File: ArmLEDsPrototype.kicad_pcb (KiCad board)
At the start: 2 copper layers, 11 parts

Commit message: Making PCB
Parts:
- added C10: C, Capacitor_SMD:C_0201_0603Metric_Pad0.64x0.40mm_HandSolder, F.Cu at (137.5, 25.7)
- added C11: C, Capacitor_SMD:C_0805_2012Metric_Pad1.18x1.45mm_HandSolder, F.Cu at (136.7, 22.5)
- added C12: C, Capacitor_SMD:C_0805_2012Metric_Pad1.18x1.45mm_HandSolder, F.Cu at (134.7, 22.5)
- added C6: C, Capacitor_SMD:C_0201_0603Metric_Pad0.64x0.40mm_HandSolder, F.Cu at (119.6, 25.2)
- added C7: C, Capacitor_SMD:C_0805_2012Metric_Pad1.18x1.45mm_HandSolder, F.Cu at (118.8, 22.0)
- added C8: C, Capacitor_SMD:C_0805_2012Metric_Pad1.18x1.45mm_HandSolder, F.Cu at (116.8, 22.0)
- added C9: C, Capacitor_SMD:C_1812_4532Metric_Pad1.57x3.40mm_HandSolder, F.Cu at (134.2, 30.4)
- added L2: L, ArmLEDFootprintLib:4r7007, F.Cu at (120.2, 23.7)
- added L3: L, ArmLEDFootprintLib:4r7007, F.Cu at (138.1, 24.2)
- added R12: R, Resistor_SMD:R_0402_1005Metric_Pad0.72x0.64mm_HandSolder, F.Cu at (114.8, 25.6)
- added R13: R, Resistor_SMD:R_0402_1005Metric_Pad0.72x0.64mm_HandSolder, F.Cu at (132.8, 23.6)
- added R14: R, Resistor_SMD:R_0402_1005Metric_Pad0.72x0.64mm_HandSolder, F.Cu at (132.7, 26.1)
- added U2: ~, ArmLEDFootprintLib:RT6254A, F.Cu at (117.2, 25.7)
- added U3: ~, ArmLEDFootprintLib:RT6254A, F.Cu at (135.1, 26.2)
- C1, C5: footprint Capacitor_SMD:C_0805_2012Metric_Pad1.18x1.45mm_HandSolder -> Capacitor_SMD:C_1812_4532Metric_Pad1.57x3.40mm_HandSolder
- L1: footprint ArmLEDFootprintLib:Inductor -> ArmLEDFootprintLib:4r7007
- moved C3 36.7 mm to (100.3, 21.2), turned to 90 degrees
- moved R10 36.2 mm to (96.3, 24.8), turned to -90 degrees
- moved R11 19.7 mm to (114.9, 23.1), turned to -90 degrees
- moved C5 17.9 mm to (116.3, 29.9), turned to 180 degrees
- moved C1 17.3 mm to (97.8, 29.1), turned to 180 degrees
- moved U1 17.2 mm to (98.7, 24.9)
- moved R9 14.9 mm to (96.4, 22.3)
- moved C4 12.3 mm to (98.3, 21.2), turned to 90 degrees
- moved L1 12.2 mm to (101.7, 22.9), turned to 90 degrees
- moved C2 10.8 mm to (101.1, 24.4), turned to -90 degrees
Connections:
- A1 pad 30: +5V -> /5V#1
- C3 pad 1: +5V -> /5V#1
- C3 pad 2: Net-(C3-Pad2) -> GND
- C4 pad 1: +5V -> /5V#1
- C5 pad 1: +5V -> +9V
- L1 pad 2: +5V -> /5V#1
- R10 pad 1: +5V -> Net-(U1-FB)
- R10 pad 2: Net-(C3-Pad2) -> GND
- R11 pad 1: GND -> /5V#2
- R11 pad 2: Net-(C3-Pad2) -> Net-(U2-FB)
- R9 pad 1: Net-(U1-FB) -> /5V#1
- R9 pad 2: Net-(C3-Pad2) -> Net-(U1-FB)
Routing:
- net +9V: track 0.00 -> 17.9 mm
- net /5V#2: track 0.00 -> 9.73 mm
- net /5V#1: track 0.00 -> 9.73 mm
- net /5V#3: track 0.00 -> 9.73 mm
- net Net-(U1-LX): track 0.00 -> 5.51 mm
- net Net-(U3-LX): track 0.00 -> 5.51 mm
- net Net-(U2-LX): track 0.00 -> 5.51 mm
- net Net-(U2-BOOT): track 0.00 -> 1.12 mm
- net Net-(U3-BOOT): track 0.00 -> 1.12 mm
- net Net-(U1-BOOT): track 0.00 -> 1.12 mm
- added copper zone on F.Cu, net GND
- added copper zone on F.Cu, net Net-(U1-LX)

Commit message: Added parts
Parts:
- added J3: Conn_01x02, Connector_Molex:Molex_Pico-EZmate_78171-0002_1x02-1MP_P1.20mm_Vertical, F.Cu at (109.2, 32.9)
- added J5: Conn_01x03, Connector_Molex:Molex_Pico-EZmate_78171-0003_1x03-1MP_P1.20mm_Vertical, F.Cu at (117.5, 32.9)
- added J6: Conn_01x02, Connector_Molex:Molex_Pico-EZmate_78171-0002_1x02-1MP_P1.20mm_Vertical, F.Cu at (101.5, 32.9)
- moved A1 85.5 mm to (139.3, 72.0), turned to 180 degrees
- moved C11 72.9 mm to (76.8, 64.0)
- moved C9 72.9 mm to (74.3, 71.9)
- moved R13 72.9 mm to (72.9, 65.1)
- moved C10 72.9 mm to (77.6, 67.2)
- moved C12 72.9 mm to (74.8, 64.0)
- moved L3 72.9 mm to (78.2, 65.7)
- moved R14 72.9 mm to (72.8, 67.6)
- moved U3 72.9 mm to (75.2, 67.7)
- moved C5 49.1 mm to (90.8, 71.9)
- moved C7 49.1 mm to (93.3, 64.0)
- moved C6 49.1 mm to (94.1, 67.2)
- moved C8 49.1 mm to (91.3, 64.0)
- moved L2 49.1 mm to (94.7, 65.7)
- moved U2 49.1 mm to (91.7, 67.7)
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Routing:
- net /5V#1: track 9.73 -> 53.4 mm
- net +9V: track 17.9 -> 55.9 mm
- net /5V#3: track 9.73 -> 46.2 mm
- net /5V#2: track 9.73 -> 42.5 mm
- net /LED_S: track 0.00 -> 26.3 mm

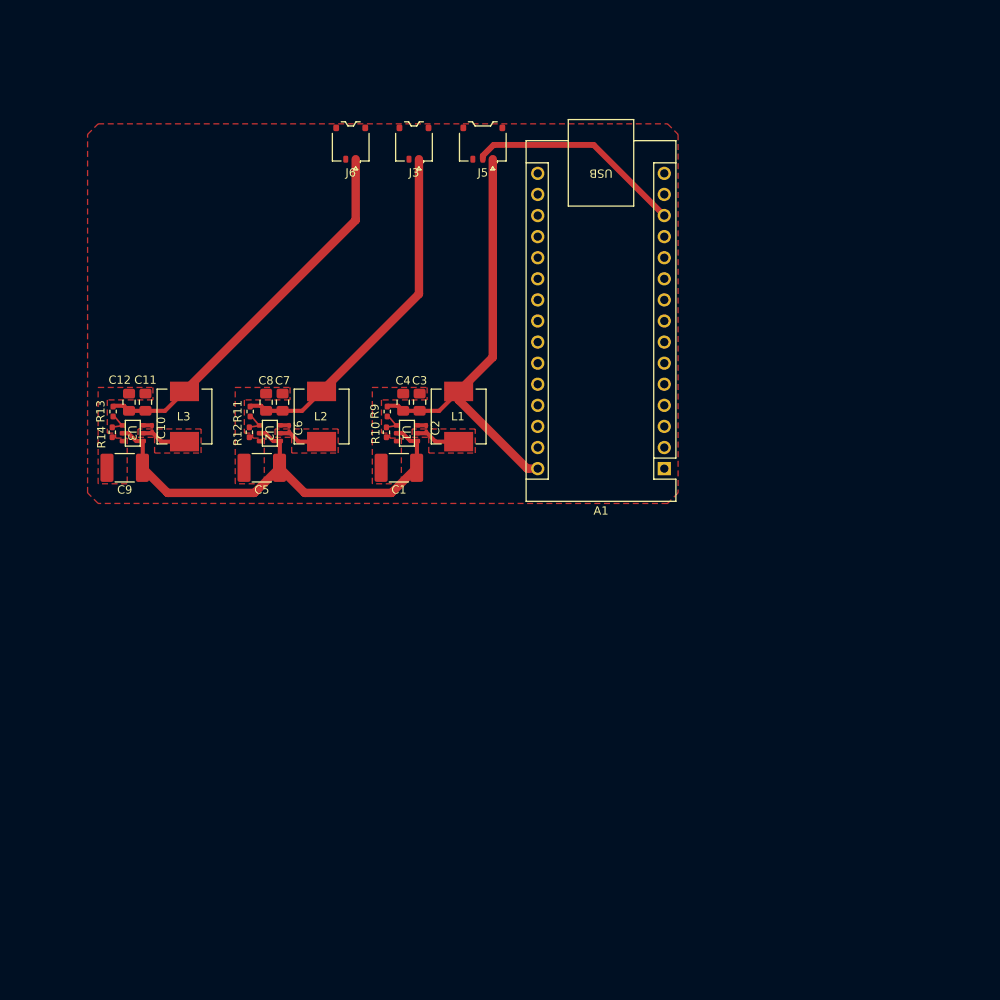
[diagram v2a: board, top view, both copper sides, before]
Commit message: Replaced switch & pots with rotaries
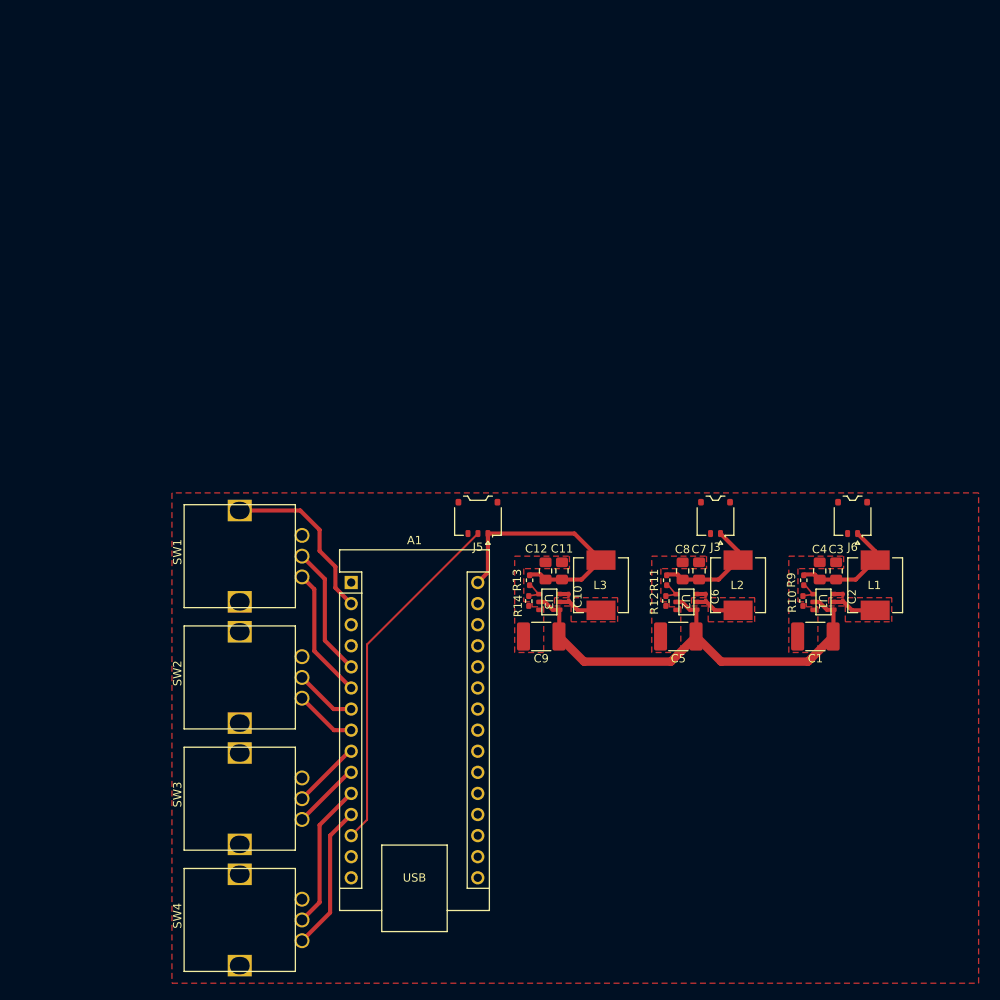
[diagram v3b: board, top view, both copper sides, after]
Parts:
- added SW1: RotaryEncoder_Switch, ArmLEDFootprintLib:RotaryEncoder, F.Cu at (81.5, 88.8)
- added SW2: RotaryEncoder, ArmLEDFootprintLib:RotaryEncoder, F.Cu at (81.5, 103.4)
- added SW3: RotaryEncoder, ArmLEDFootprintLib:RotaryEncoder, F.Cu at (81.5, 118.0)
- added SW4: RotaryEncoder, ArmLEDFootprintLib:RotaryEncoder, F.Cu at (81.5, 132.6)
- moved J6 75.4 mm to (162.0, 78.0)
- moved J3 57.9 mm to (145.5, 78.0)
- moved C2 54.1 mm to (160.8, 87.5)
- moved C4 54.1 mm to (158.0, 84.3)
- moved C5 54.1 mm to (141.0, 92.2)
- moved C7 54.1 mm to (143.5, 84.3)
- moved L1 54.1 mm to (161.4, 86.0)
- moved L2 54.1 mm to (144.9, 86.0)
- moved R12 54.1 mm to (139.5, 88.0)
- moved R14 54.1 mm to (123.0, 88.0)
- moved U1 54.1 mm to (158.4, 88.0)
- moved U2 54.1 mm to (141.9, 88.0)
- moved U3 54.1 mm to (125.4, 88.0)
- moved C1 54.1 mm to (157.5, 92.2)
- moved C9 54.1 mm to (124.5, 92.2)
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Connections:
- A1 pad 1: Net-(A1-TX1) -> unconnected-(A1-TX1-Pad1)
- A1 pad 10: /DIPSwitches/SW6 -> /Controller/Input3A
- A1 pad 11: /DIPSwitches/SW7 -> /Controller/Input4B
- A1 pad 12: /DIPSwitches/SW8 -> /Controller/Input4A
- A1 pad 19: /Tuner/Out1 -> unconnected-(A1-A0-Pad19)
- A1 pad 2: Net-(A1-RX1) -> /Controller/InputS
- A1 pad 20: /Tuner/Out2 -> unconnected-(A1-A1-Pad20)
- A1 pad 21: /Tuner/Out3 -> unconnected-(A1-A2-Pad21)
- A1 pad 30: /5V#1 -> /5V#3
- A1 pad 5: /DIPSwitches/SW1 -> /Controller/Input1B
- A1 pad 6: /DIPSwitches/SW2 -> /Controller/Input1A
- A1 pad 7: /DIPSwitches/SW3 -> /Controller/Input2B
- A1 pad 8: /DIPSwitches/SW4 -> /Controller/Input2A
- A1 pad 9: /DIPSwitches/SW5 -> /Controller/Input3B
- J5 pad 1: /5V#1 -> /5V#3
- J6 pad 1: /5V#3 -> /5V#1
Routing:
- net /5V#1: track 53.4 -> 14.7 mm
- net /5V#2: track 42.5 -> 13.8 mm
- net /Controller/InputS: track 0.00 -> 21.0 mm
- net /Controller/Input4B: track 0.00 -> 17.7 mm
- net /Controller/Input4A: track 0.00 -> 17.7 mm
- net /LED_S: track 26.3 -> 42.7 mm
- net /Controller/Input1A: track 0.00 -> 15.8 mm
- net /Controller/Input1B: track 0.00 -> 15.8 mm
- net /5V#3: track 46.2 -> 31.1 mm
- net /Controller/Input3B: track 0.00 -> 8.29 mm
- net /Controller/Input3A: track 0.00 -> 8.28 mm
- net /Controller/Input2A: track 0.00 -> 7.52 mm
- net /Controller/Input2B: track 0.00 -> 7.50 mm

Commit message: Added information
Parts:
- added J1: Conn_01x08, ArmLEDFootprintLib:8Pad, F.Cu at (122.3, 131.3)
- moved A1 6.19 mm to (102.6, 91.8)
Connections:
- A1 pad 19: unconnected-(A1-A0-Pad19) -> Net-(A1-A0)
- A1 pad 20: unconnected-(A1-A1-Pad20) -> Net-(A1-A1)
- A1 pad 21: unconnected-(A1-A2-Pad21) -> Net-(A1-A2)
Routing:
- net Net-(A1-A7): track 0.00 -> 61.0 mm
- net Net-(A1-A6): track 0.00 -> 53.6 mm
- net Net-(A1-SCL/A5): track 0.00 -> 46.2 mm
- net Net-(A1-SDA/A4): track 0.00 -> 38.8 mm
- net Net-(A1-A3): track 0.00 -> 31.4 mm
- net Net-(A1-A2): track 0.00 -> 25.6 mm
- net Net-(A1-A1): track 0.00 -> 19.8 mm
- net Net-(A1-A0): track 0.00 -> 13.4 mm
- net /Controller/Input1A: track 15.8 -> 22.4 mm
- net /Controller/Input1B: track 15.8 -> 22.3 mm
- net /Controller/InputS: track 21.0 -> 27.6 mm
- net /LED_S: track 42.7 -> 48.4 mm
- net /5V#3: track 31.1 -> 36.8 mm
- net /Controller/Input4B: track 17.7 -> 12.0 mm
- net /Controller/Input4A: track 17.7 -> 12.0 mm
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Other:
- board text added: "2082940020"
- board text added: "2082940030"
- board text added: "A0"
- board text added: "A1"
- board text added: "A2"
- board text added: "A3"
- board text added: "A4"
- board text added: "A5"
- board text added: "A6"
- board text added: "A7"
- board text added: "Arduino Nano"
- board text added: "ArmLED - 2024 v2.0"
- board text added: "Brendan Lee"
- board text added: "Main Connector"
- board text added: "PEC12R- 4220F- S0024"
- board text added: "Team 1540"
- board text added: "Voltage Regulator Parts C1: 18123C284KAT2A C2: CL10B104KO8NNNC C3 C4: CL21A226KQCLRNC R9 R10: PNM0402E5001BST1 L1: 0630CDMCCDS-4R7MC U1: RT6254BHGJ6F 500kHz 12V to 5V 4A> current draw"

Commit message: Fixed wiring mistake + information
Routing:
- net /Controller/Input1B: track 22.3 -> 24.8 mm
- net /Controller/Input2B: track 12.8 -> 15.3 mm
- net /Controller/Input4B: track 12.0 -> 9.71 mm
- net /Controller/Input3B: track 7.11 -> 8.15 mm
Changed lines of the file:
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@@
 		)
 		(pad "B" thru_hole circle
-			(at 6.2 14.2 180)
+			(at 8.7 14.2 180)
 			(size 1.8 1.8)
 			(drill 1.3)
@@
 		)
 		(pad "C" thru_hole circle
-			(at 8.7 14.2 180)
+			(at 6.2 14.2 180)
 			(size 1.8 1.8)
 			(drill 1.3)
@@
 		)
 		(pad "B" thru_hole circle
-			(at 6.2 14.2 180)
+			(at 8.7 14.2 180)
 			(size 1.8 1.8)
 			(drill 1.3)
@@
 		)
 		(pad "C" thru_hole circle
-			(at 8.7 14.2 180)
+			(at 6.2 14.2 180)
 			(size 1.8 1.8)
 			(drill 1.3)
@@
 		)
 		(pad "B" thru_hole circle
-			(at 6.2 14.2 180)
+			(at 8.7 14.2 180)
 			(size 1.8 1.8)
 			(drill 1.3)
@@
 		)
 		(pad "C" thru_hole circle
-			(at 8.7 14.2 180)
+			(at 6.2 14.2 180)
 			(size 1.8 1.8)
 			(drill 1.3)
@@
 		)
 		(pad "B" thru_hole circle
-			(at 6.2 14.2 180)
+			(at 8.7 14.2 180)
 			(size 1.8 1.8)
 			(drill 1.3)
@@
 		)
 		(pad "C" thru_hole circle
-			(at 8.7 14.2 180)
+			(at 6.2 14.2 180)
 			(size 1.8 1.8)
 			(drill 1.3)
@@
 	)
 	(segment
-		(start 98.044 121.811)
-		(end 102.63 117.225)
+		(start 102.63 117.225)
+		(end 95.99 123.865)
 		(width 0.5)
 		(layer "F.Cu")
@@
 	)
 	(segment
-		(start 95.675 126.365)
-		(end 98.044 123.996)
+		(start 95.99 123.865)
+		(end 95.675 123.865)
 		(width 0.5)
 		(layer "F.Cu")
@@
 	)
 	(segment
-		(start 98.044 123.996)
-		(end 98.044 121.811)
-		(width 0.5)
-		(layer "F.Cu")
-		(net 31)
-	)
-	(segment
-		(start 95.675 128.865)
-		(end 99.568 124.972)
+		(start 99.314 123.081)
+		(end 99.314 125.226)
 		(width 0.5)
 		(layer "F.Cu")
@@
 	)
 	(segment
-		(start 99.568 124.972)
-		(end 99.568 122.827)
+		(start 99.314 125.226)
+		(end 95.675 128.865)
 		(width 0.5)
 		(layer "F.Cu")
@@
 	)
 	(segment
-		(start 99.568 122.827)
-		(end 102.63 119.765)
+		(start 102.63 119.765)
+		(end 99.314 123.081)
 		(width 0.5)
 		(layer "F.Cu")
@@
 	)
 	(segment
-		(start 95.465 77.05)
-		(end 101.03 82.615)
+		(start 95.592 77.05)
+		(end 88.175 77.05)
 		(width 0.5)
 		(layer "F.Cu")
@@
 	)
 	(segment
-		(start 101.03 92.765)
-		(end 102.63 94.365)
+		(start 101.092 82.55)
+		(end 95.592 77.05)
 		(width 0.5)
 		(layer "F.Cu")
@@
 	)
 	(segment
-		(start 88.175 77.05)
-		(end 95.465 77.05)
+		(start 102.239 94.365)
+		(end 101.092 93.218)
 		(width 0.5)
 		(layer "F.Cu")
@@
 	)
 	(segment
-		(start 101.03 82.615)
-		(end 101.03 92.765)
+		(start 101.092 93.218)
+		(end 101.092 82.55)
 		(width 0.5)
 		(layer "F.Cu")
@@
 	)
 	(segment
-		(start 99.76 86.635)
-		(end 99.76 99.115)
+		(start 102.63 94.365)
+		(end 102.239 94.365)
 		(width 0.5)
 		(layer "F.Cu")
-		(net 34)
+		(net 33)
 	)
 	(segment
-		(start 95.675 82.55)
-		(end 99.76 86.635)
+		(start 99.822 99.177)
+		(end 99.822 84.197)
 		(width 0.5)
 		(layer "F.Cu")
@@
 	)
 	(segment
-		(start 99.76 99.115)
-		(end 102.63 101.985)
+		(start 102.63 101.985)
+		(end 99.822 99.177)
 		(width 0.5)
 		(layer "F.Cu")
@@
 	)
 	(segment
-		(start 102.63 104.408)
-		(end 102.63 104.525)
+		(start 99.822 84.197)
+		(end 95.675 80.05)
 		(width 0.5)
 		(layer "F.Cu")
-		(net 35)
+		(net 34)
 	)
 	(segment
-		(start 95.675 85.05)
+		(start 98.552 100.447)
 		(end 98.552 87.927)
 		(width 0.5)
@@
 	)
 	(segment
-		(start 98.552 100.33)
-		(end 102.63 104.408)
+		(start 98.552 87.927)
+		(end 95.675 85.05)
 		(width 0.5)
 		(layer "F.Cu")
@@
 	)
 	(segment
-		(start 98.552 87.927)
-		(end 98.552 100.33)
+		(start 102.63 104.525)
+		(end 98.552 100.447)
 		(width 0.5)
 		(layer "F.Cu")
@@
 	)
 	(segment
-		(start 95.675 111.76)
-		(end 102.245 111.76)
+		(start 98.56 112.145)
+		(end 102.63 112.145)
 		(width 0.5)
 		(layer "F.Cu")
@@
 	)
 	(segment
-		(start 102.245 111.76)
-		(end 102.63 112.145)
+		(start 95.675 109.26)
+		(end 98.56 112.145)
 		(width 0.5)
 		(layer "F.Cu")
@@
 	)
 	(segment
-		(start 95.675 114.26)
-		(end 102.205 114.26)
+		(start 102.205 114.26)
+		(end 102.63 114.685)
 		(width 0.5)
 		(layer "F.Cu")
@@
 	)
 	(segment
-		(start 102.205 114.26)
-		(end 102.63 114.685)
+		(start 95.675 114.26)
+		(end 102.205 114.26)
 		(width 0.5)
 		(layer "F.Cu")
@@
 	)
 	(segment
-		(start 97.536 101.971)
-		(end 102.63 107.065)
+		(start 95.675 94.655)
+		(end 97.536 96.516)
 		(width 0.5)
 		(layer "F.Cu")
@@
 	)
 	(segment
-		(start 97.536 99.016)
+		(start 97.536 96.516)
 		(end 97.536 101.971)
 		(width 0.5)
@@
 	)
 	(segment
-		(start 95.675 97.155)
-		(end 97.536 99.016)
+		(start 97.536 101.971)
+		(end 102.63 107.065)
 		(width 0.5)
 		(layer "F.Cu")
@@
 			(thermal_gap 0.5)
 			(thermal_bridge_width 0.5)
-			(island_removal_mode 1)
-			(island_area_min 9.999999)
 		)
 		(polygon
